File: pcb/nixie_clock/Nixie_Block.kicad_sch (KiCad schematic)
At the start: 26 parts, among them U66 MSD42WT1G, U67 MSD42WT1G, U68 MSD42WT1G, U69 MSD42WT1G, U70 MSD42WT1G, U71 MSD42WT1G, U72 MSD42WT1G, U73 MSD42WT1G, U74 MSD42WT1G, U75 MSD42WT1G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

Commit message: remove busses and output stuff
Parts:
- removed R72: 2K2, symbol Device:R
- R66, R73: value 1K -> 7K87
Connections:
- net +170V: now also V6.1 (Anode)

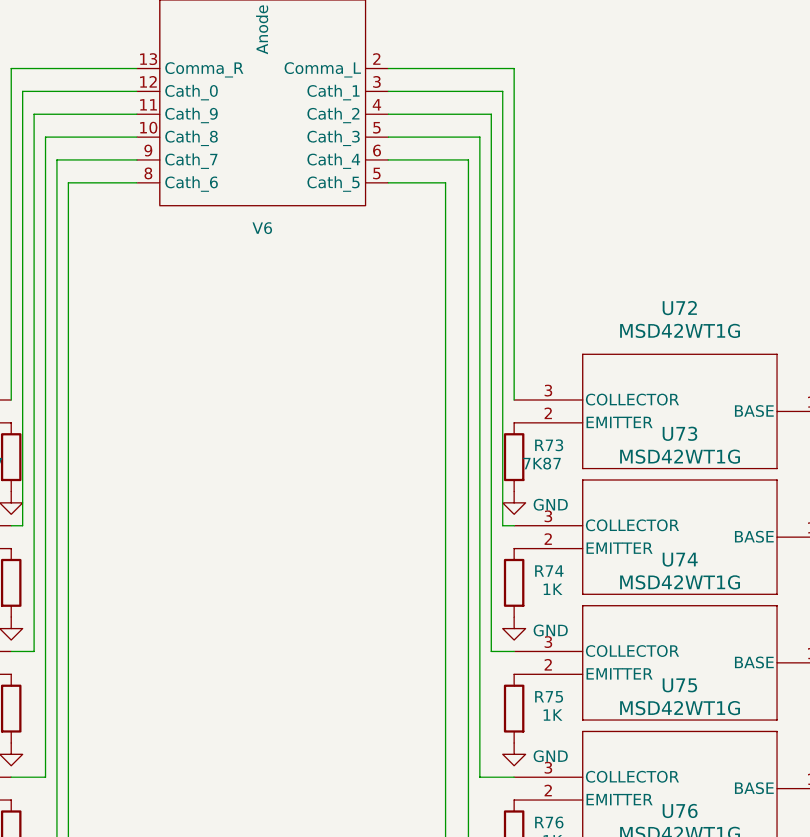
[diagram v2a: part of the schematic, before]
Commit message: schematic finalisation, footprint assignment and start on placeing components in layout.
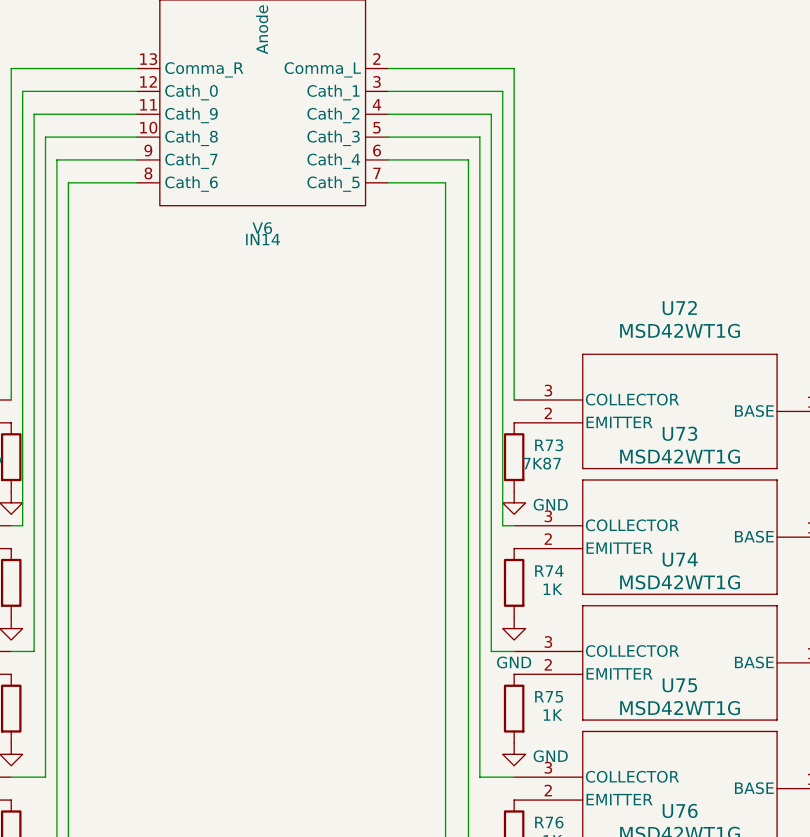
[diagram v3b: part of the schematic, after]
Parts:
- R66, R67, R68, R69, R70, R71, R73, R74, R75, R76, R77, R78: footprint (none) -> Resistor_SMD:R_0603_1608Metric
- V6: value ~ -> IN14; footprint (none) -> Nixie_Stuff:IN14
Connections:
- net at U77.3 (COLLECTOR): now also V6.7 (Cath_5); no longer V6.5 (Cath_5)

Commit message: finalization of schematic (might add fuze on 170v supply) looking at pcb routing now. Decided on 6 layers.
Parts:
- U66, U67, U68, U69, U70, U71, U72, U73, U74, U75, U76, U77: footprint SOT-323-3_2P2X1P35_ONS -> footprints:SOT-323-3_2P2X1P35_ONS
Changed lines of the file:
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@@
 			)
 		)
-		(property "Footprint" "SOT-323-3_2P2X1P35_ONS"
+		(property "Footprint" "footprints:SOT-323-3_2P2X1P35_ONS"
 			(at 22.606 129.54 0)
 			(effects
@@
 			)
 		)
-		(property "Footprint" "SOT-323-3_2P2X1P35_ONS"
+		(property "Footprint" "footprints:SOT-323-3_2P2X1P35_ONS"
 			(at 22.606 143.51 0)
 			(effects
@@
 			)
 		)
-		(property "Footprint" "SOT-323-3_2P2X1P35_ONS"
+		(property "Footprint" "footprints:SOT-323-3_2P2X1P35_ONS"
 			(at 22.606 157.48 0)
 			(effects
@@
 			)
 		)
-		(property "Footprint" "SOT-323-3_2P2X1P35_ONS"
+		(property "Footprint" "footprints:SOT-323-3_2P2X1P35_ONS"
 			(at 180.594 157.48 0)
 			(effects
@@
 			)
 		)
-		(property "Footprint" "SOT-323-3_2P2X1P35_ONS"
+		(property "Footprint" "footprints:SOT-323-3_2P2X1P35_ONS"
 			(at 180.594 143.51 0)
 			(effects
@@
 			)
 		)
-		(property "Footprint" "SOT-323-3_2P2X1P35_ONS"
+		(property "Footprint" "footprints:SOT-323-3_2P2X1P35_ONS"
 			(at 22.606 87.63 0)
 			(effects
@@
 			)
 		)
-		(property "Footprint" "SOT-323-3_2P2X1P35_ONS"
+		(property "Footprint" "footprints:SOT-323-3_2P2X1P35_ONS"
 			(at 180.594 129.54 0)
 			(effects
@@
 			)
 		)
-		(property "Footprint" "SOT-323-3_2P2X1P35_ONS"
+		(property "Footprint" "footprints:SOT-323-3_2P2X1P35_ONS"
 			(at 180.594 115.57 0)
 			(effects
@@
 			)
 		)
-		(property "Footprint" "SOT-323-3_2P2X1P35_ONS"
+		(property "Footprint" "footprints:SOT-323-3_2P2X1P35_ONS"
 			(at 22.606 101.6 0)
 			(effects
@@
 			)
 		)
-		(property "Footprint" "SOT-323-3_2P2X1P35_ONS"
+		(property "Footprint" "footprints:SOT-323-3_2P2X1P35_ONS"
 			(at 180.594 87.63 0)
 			(effects
@@
 			)
 		)
-		(property "Footprint" "SOT-323-3_2P2X1P35_ONS"
+		(property "Footprint" "footprints:SOT-323-3_2P2X1P35_ONS"
 			(at 22.606 115.57 0)
 			(effects
@@
 			)
 		)
-		(property "Footprint" "SOT-323-3_2P2X1P35_ONS"
+		(property "Footprint" "footprints:SOT-323-3_2P2X1P35_ONS"
 			(at 180.594 101.6 0)
 			(effects

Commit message: 3d models done
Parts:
- R66, R73: LCSC Part # (none) -> RC0603FR-077K87L
- R67, R68, R69, R70, R71, R74, R75, R76, R77, R78: LCSC Part # (none) -> C22548
- U66, U67, U68, U69, U70, U71, U72, U73, U74, U75, U76, U77: LCSC Part # (none) -> C891781
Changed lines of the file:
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@@
 			)
 		)
+		(property "LCSC Part #" "C22548"
+			(at 73.66 138.43 0)
+			(effects
+				(font
+					(size 1.27 1.27)
+				)
+				(hide yes)
+			)
+		)
 		(pin "2"
 		)
@@
 			)
 		)
+		(property "LCSC Part #" "C22548"
+			(at 129.54 124.46 0)
+			(effects
+				(font
+					(size 1.27 1.27)
+				)
+				(hide yes)
+			)
+		)
 		(pin "2"
 		)
@@
 			)
 		)
+		(property "LCSC Part #" "C891781"
+			(at 22.86 132.08 0)
+			(effects
+				(font
+					(size 1.27 1.27)
+				)
+				(hide yes)
+			)
+		)
 		(pin "3"
 		)
@@
 			)
 		)
+		(property "LCSC Part #" "C891781"
+			(at 22.86 146.05 0)
+			(effects
+				(font
+					(size 1.27 1.27)
+				)
+				(hide yes)
+			)
+		)
 		(pin "3"
 		)
@@
 			)
 		)
+		(property "LCSC Part #" "C22548"
+			(at 129.54 166.37 0)
+			(effects
+				(font
+					(size 1.27 1.27)
+				)
+				(hide yes)
+			)
+		)
 		(pin "2"
 		)
@@
 			)
 		)
+		(property "LCSC Part #" "C891781"
+			(at 22.86 160.02 0)
+			(effects
+				(font
+					(size 1.27 1.27)
+				)
+				(hide yes)
+			)
+		)
 		(pin "3"
 		)
@@
 			)
 		)
+		(property "LCSC Part #" "C891781"
+			(at 180.34 160.02 0)
+			(effects
+				(font
+					(size 1.27 1.27)
+				)
+				(hide yes)
+			)
+		)
 		(pin "3"
 		)
@@
 			)
 		)
+		(property "LCSC Part #" "C891781"
+			(at 180.34 146.05 0)
+			(effects
+				(font
+					(size 1.27 1.27)
+				)
+				(hide yes)
+			)
+		)
 		(pin "3"
 		)
@@
 			)
 		)
+		(property "LCSC Part #" "RC0603FR-077K87L"
+			(at 73.66 96.52 0)
+			(effects
+				(font
+					(size 1.27 1.27)
+				)
+				(hide yes)
+			)
+		)
 		(pin "2"
 		)
@@
 			)
 		)
+		(property "LCSC Part #" "RC0603FR-077K87L"
+			(at 129.54 96.52 0)
+			(effects
+				(font
+					(size 1.27 1.27)
+				)
+				(hide yes)
+			)
+		)
 		(pin "2"
 		)
@@
 			)
 		)
+		(property "LCSC Part #" "C22548"
+			(at 129.54 110.49 0)
+			(effects
+				(font
+					(size 1.27 1.27)
+				)
+				(hide yes)
+			)
+		)
 		(pin "2"
 		)
@@
 			)
 		)
+		(property "LCSC Part #" "C891781"
+			(at 22.86 90.17 0)
+			(effects
+				(font
+					(size 1.27 1.27)
+				)
+				(hide yes)
+			)
+		)
 		(pin "3"
 		)
@@
 			)
 		)
+		(property "LCSC Part #" "C22548"
+			(at 73.66 152.4 0)
+			(effects
+				(font
+					(size 1.27 1.27)
+				)
+				(hide yes)
+			)
+		)
 		(pin "2"
 		)
@@
 			)
 		)
+		(property "LCSC Part #" "C891781"
+			(at 180.34 132.08 0)
+			(effects
+				(font
+					(size 1.27 1.27)
+				)
+				(hide yes)
+			)
+		)
 		(pin "3"
 		)
@@
 			)
 		)
+		(property "LCSC Part #" "C22548"
+			(at 129.54 152.4 0)
+			(effects
+				(font
+					(size 1.27 1.27)
+				)
+				(hide yes)
+			)
+		)
 		(pin "2"
 		)
@@
 			)
 		)
+		(property "LCSC Part #" "C891781"
+			(at 180.34 118.11 0)
+			(effects
+				(font
+					(size 1.27 1.27)
+				)
+				(hide yes)
+			)
+		)
 		(pin "3"
 		)
@@
 			)
 		)
+		(property "LCSC Part #" "C891781"
+			(at 22.86 104.14 0)
+			(effects
+				(font
+					(size 1.27 1.27)
+				)
+				(hide yes)
+			)
+		)
 		(pin "3"
 		)
@@
 			)
 		)
+		(property "LCSC Part #" "C22548"
+			(at 73.66 124.46 0)
+			(effects
+				(font
+					(size 1.27 1.27)
+				)
+				(hide yes)
+			)
+		)
 		(pin "2"
 		)
@@
 			)
 		)
+		(property "LCSC Part #" "C891781"
+			(at 180.34 90.17 0)
+			(effects
+				(font
+					(size 1.27 1.27)
+				)
+				(hide yes)
+			)
+		)
 		(pin "3"
 		)
@@
 			)
 		)
+		(property "LCSC Part #" "C891781"
+			(at 22.86 118.11 0)
+			(effects
+				(font
+					(size 1.27 1.27)
+				)
+				(hide yes)
+			)
+		)
 		(pin "3"
 		)
@@
 			)
 		)
+		(property "LCSC Part #" "C22548"
+			(at 129.54 138.43 0)
+			(effects
+				(font
+					(size 1.27 1.27)
+				)
+				(hide yes)
+			)
+		)
 		(pin "2"
 		)
@@
 			)
 		)
+		(property "LCSC Part #" "C22548"
+			(at 73.66 110.49 0)
+			(effects
+				(font
+					(size 1.27 1.27)
+				)
+				(hide yes)
+			)
+		)
 		(pin "2"
 		)
@@
 			)
 		)
+		(property "LCSC Part #" "C22548"
+			(at 73.66 166.37 0)
+			(effects
+				(font
+					(size 1.27 1.27)
+				)
+				(hide yes)
+			)
+		)
 		(pin "2"
 		)
@@
 			(at 180.34 104.14 0)
 			(effects
+				(font
+					(size 1.27 1.27)
+				)
+				(hide yes)
+			)
+		)
+		(property "LCSC Part #" "C891781"
+			(at 180.34 104.14 0)
+			(effects

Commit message: fixing some issues.
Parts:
- R66, R73: LCSC Part # RC0603FR-077K87L -> C137680
- V6: now not fitted
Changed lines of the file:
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@@
 			)
 		)
-		(property "LCSC Part #" "RC0603FR-077K87L"
+		(property "LCSC Part #" "C137680"
 			(at 73.66 96.52 0)
 			(effects
@@
 			)
 		)
-		(property "LCSC Part #" "RC0603FR-077K87L"
+		(property "LCSC Part #" "C137680"
 			(at 129.54 96.52 0)
 			(effects
@@
 		(in_bom yes)
 		(on_board yes)
-		(dnp no)
+		(dnp yes)
 		(property "Reference" "V6"
 			(at 101.6 71.12 0)

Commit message: added grounding
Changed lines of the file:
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@@
 	(wire
 		(pts
-			(xy 129.54 160.02) (xy 121.92 160.02)
+			(xy 129.54 160.02) (xy 123.19 160.02)
 		)
 		(stroke
@@
 	(wire
 		(pts
-			(xy 121.92 160.02) (xy 121.92 66.04)
+			(xy 123.19 160.02) (xy 123.19 66.04)
 		)
 		(stroke
@@
 	(wire
 		(pts
-			(xy 121.92 66.04) (xy 115.57 66.04)
+			(xy 123.19 66.04) (xy 115.57 66.04)
 		)
 		(stroke
